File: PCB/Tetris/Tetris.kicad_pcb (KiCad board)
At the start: 2 copper layers, 49 parts, among them J1 Power, J2 PWM, J3 Analog, J4 PWM, J5 Analog, J6 Communication, J7 Digital, M1 RGBMatrix, M2 RGBMatrix, SW1 SW_Push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

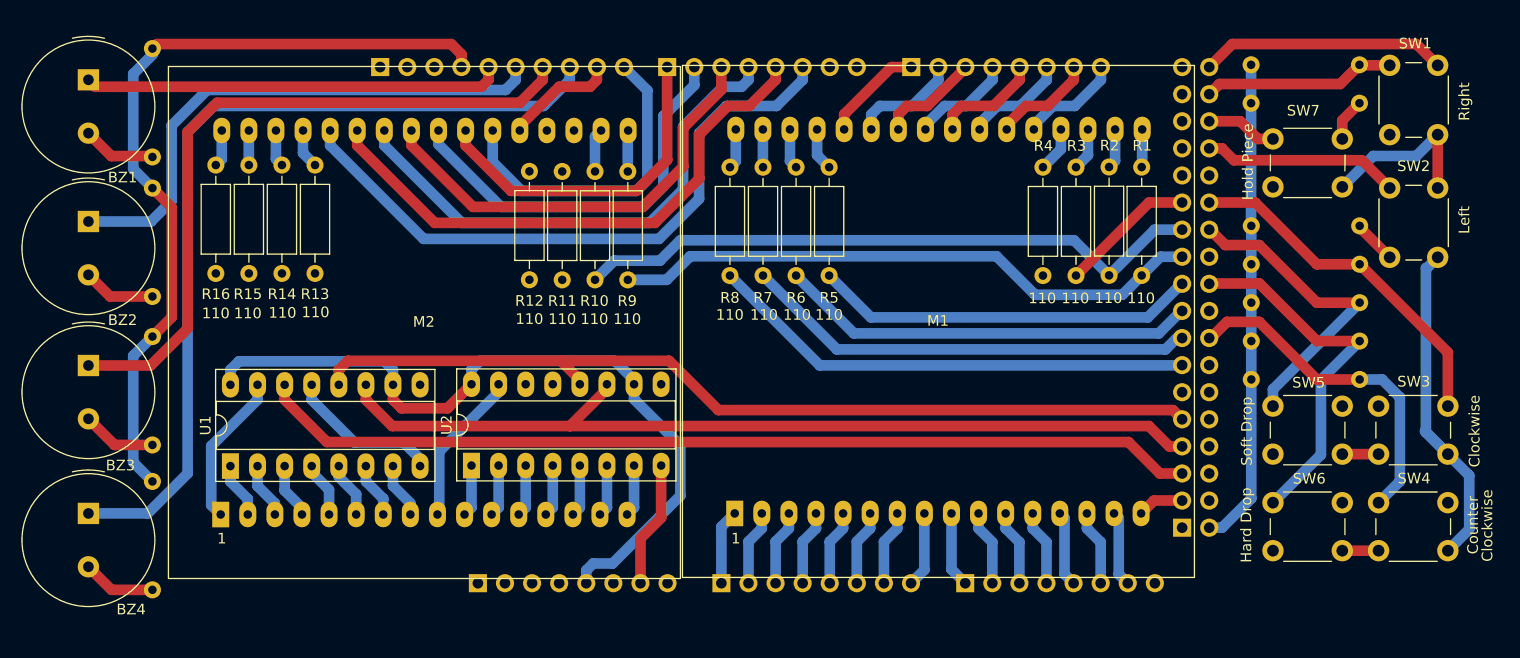
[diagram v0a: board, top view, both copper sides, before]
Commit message: Finished PCB
Finish PCB,
will still have to double check it
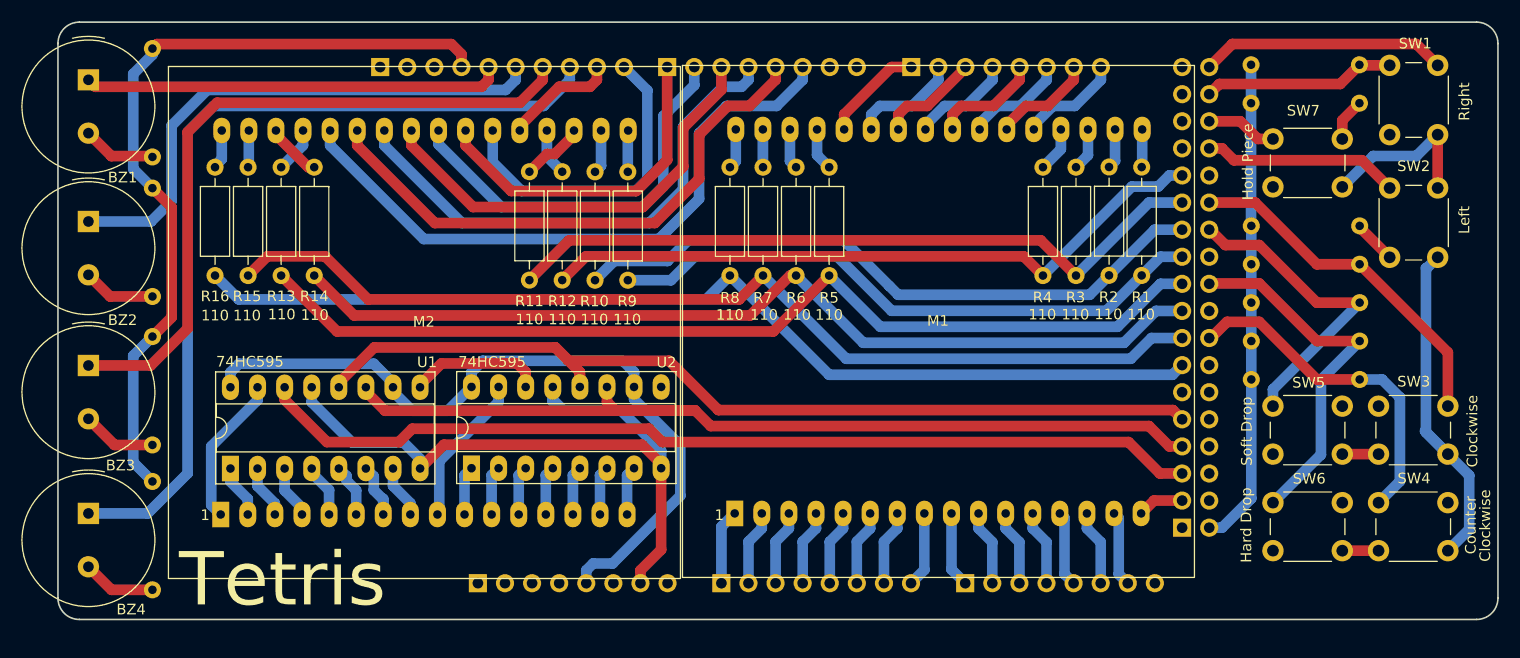
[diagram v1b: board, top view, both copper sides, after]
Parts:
- moved R13 3.18 mm to (103.9, 91.6)
- moved R12 3.08 mm to (130.3, 102.2)
- moved R11 3.08 mm to (127.2, 102.2)
- moved R14 3.03 mm to (107.0, 91.6)
- moved U2 0.25 mm to (121.8, 119.8)
- moved U1 0.23 mm to (99.2, 119.8)
- moved R15 0.21 mm to (100.8, 91.6)
- moved R16 0.21 mm to (97.7, 91.6)
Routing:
- net /28: track 0.00 -> 63.7 mm
- net /36: track 36.0 -> 92.5 mm
- net /30: track 12.8 -> 66.9 mm
- net /40: track 42.6 -> 94.9 mm
- net /42: track 45.9 -> 96.7 mm
- net /38: track 39.3 -> 88.3 mm
- net GND: track 147.9 -> 189.8 mm
- net Net-(U1-QH'): track 0.00 -> 12.5 mm
- net Net-(M2-P_3): track 0.00 -> 6.02 mm
- net Net-(M2-P_4): track 0.00 -> 4.46 mm
- net /48: track 85.1 -> 89.1 mm
- net /*46: track 86.0 -> 89.9 mm
- net Net-(M2-P_6): track 3.57 -> 5.25 mm
- net /32: track 59.7 -> 61.2 mm
- net /S7: track 5.21 -> 6.47 mm
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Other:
- board outline added: 135 x 56 mm
- board text added: "Jonathan Cai 2023"
- board text added: "Tetris"

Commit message: Added funnyjoke
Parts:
- added G1: LOGO, LOGO, F.Cu at (165.8, 95.7)
- added Mr. G: LOGO, LOGO, F.Cu at (165.3, 106.7)

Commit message: Sync changes
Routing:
- net /23: track 18.0 -> 32.2 mm
- net GND: track 189.8 -> 188.9 mm

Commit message: Sync Changes
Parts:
- moved R2 3.40 mm to (178.2, 102.6)
- moved R3 3.40 mm to (175.1, 102.6)
- moved R1 3.40 mm to (181.3, 102.6)
- moved R4 3.40 mm to (172.0, 102.6)
- moved G1 2.09 mm to (163.7, 95.8)
- moved Mr. G 2.01 mm to (163.3, 106.9)
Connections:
- R1 pad 1: /34 -> /28
- R10 pad 1: /32 -> /26
- R11 pad 1: /30 -> /24
- R12 pad 1: /28 -> /22
- R13 pad 2: /36 -> /30
- R14 pad 2: /38 -> /32
- R15 pad 2: /40 -> /34
- R16 pad 2: /42 -> /36
- R2 pad 1: /32 -> /26
- R3 pad 1: /30 -> /24
- R4 pad 1: /28 -> /22
- R5 pad 2: /36 -> /30
- R6 pad 2: /38 -> /32
- R7 pad 2: /40 -> /34
- R8 pad 2: /42 -> /36
- R9 pad 1: /34 -> /28
- U1 pad 11: /48 -> /42
- U1 pad 12: /*46 -> /40
- U1 pad 14: /50 -> /*44
- U1 pad 9: Net-(U1-QH') -> unconnected-(U1-QH'-Pad9)
- U2 pad 11: /48 -> /*46
- U2 pad 12: /*46 -> /48
- U2 pad 14: Net-(U1-QH') -> /50
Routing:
- net /38: track 88.3 -> 0.00 mm
- net /*44: track 0.00 -> 87.7 mm
- net /24: track 0.00 -> 72.0 mm
- net /22: track 0.00 -> 70.0 mm
- net /26: track 0.00 -> 66.8 mm
- net /30: track 66.9 -> 113.0 mm
- net /34: track 57.1 -> 98.4 mm
- net /*46: track 89.9 -> 56.0 mm
- net /32: track 61.2 -> 92.0 mm
- net /48: track 89.1 -> 59.3 mm
- net /50: track 89.2 -> 65.1 mm
- net /42: track 96.7 -> 77.7 mm
- net /40: track 94.9 -> 81.2 mm
- net Net-(U1-QH'): track 12.5 -> 0.00 mm
- net /23: track 32.2 -> 20.9 mm
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
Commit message: snyc
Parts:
- moved G1 0.35 mm to (164.0, 96.0)
- moved Mr. G 0.35 mm to (163.6, 107.1)
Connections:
- R1 pad 1: /28 -> /30
- R10 pad 1: /26 -> /28
- R11 pad 1: /24 -> /26
- R12 pad 1: /22 -> /24
- R13 pad 2: /30 -> /32
- R14 pad 2: /32 -> /34
- R15 pad 2: /34 -> /36
- R16 pad 2: /36 -> /38
- R2 pad 1: /26 -> /28
- R3 pad 1: /24 -> /26
- R4 pad 1: /22 -> /24
- R5 pad 2: /30 -> /32
- R6 pad 2: /32 -> /34
- R7 pad 2: /34 -> /36
- R8 pad 2: /36 -> /38
- R9 pad 1: /28 -> /30
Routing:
- net /38: track 0.00 -> 98.3 mm
- net /22: track 70.0 -> 0.00 mm
- net /30: track 113.0 -> 60.6 mm
- net /34: track 98.4 -> 89.9 mm
- net /32: track 92.0 -> 99.3 mm
- net /24: track 72.0 -> 67.9 mm
- net /26: track 66.8 -> 70.6 mm
- net /36: track 99.4 -> 96.5 mm
- net /28: track 63.5 -> 64.7 mm
- net GND: track 180.0 -> 181.0 mm
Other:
- board text added: "TETRIS"
- board text removed: "Tetris"
